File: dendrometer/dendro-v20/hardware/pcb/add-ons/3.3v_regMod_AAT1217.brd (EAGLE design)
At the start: 13.5 x 11.2 mm, 7 parts, among them J1 MF-CON-2.54mm-01x03, J2 CON_01X01LUX, U1 AAT1217-SOT23-6

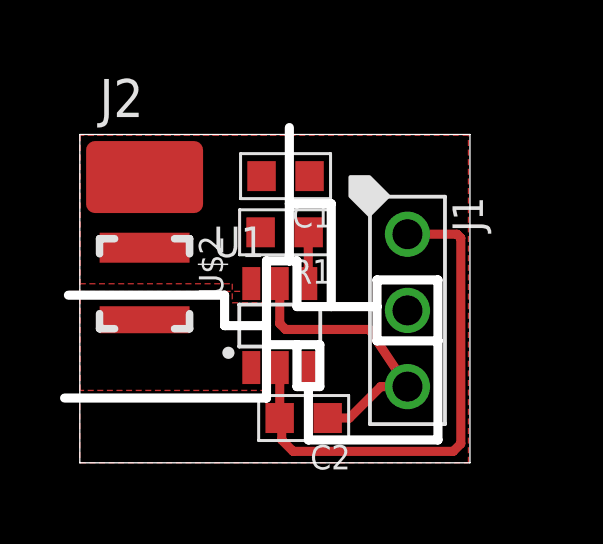
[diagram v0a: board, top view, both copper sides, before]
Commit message: making add-on boards for dendro upgrades)
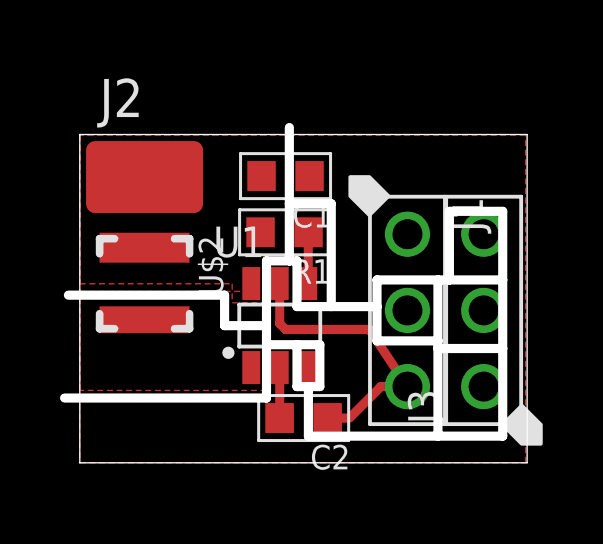
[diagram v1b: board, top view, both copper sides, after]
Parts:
- added J3: MF-CON-2.54mm-01x03, My_Connectors:PTH_2.54MM_01X03
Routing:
- net GND: track 17.4 -> 1.68 mm
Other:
- board size 13.5 x 11.2 mm -> 15.4 x 11.2 mm
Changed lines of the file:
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@@
 <?xml version="1.0" encoding="utf-8"?>
 <!DOCTYPE eagle SYSTEM "eagle.dtd">
-<eagle version="8.0.0">
+<eagle version="8.0.1">
 <drawing>
 <settings>
@@
 <board>
 <plain>
-<wire x1="0" y1="0" x2="13.005" y2="0" width="0" layer="20"/>
-<wire x1="13.005" y1="0" x2="13.005" y2="10.94375" width="0" layer="20"/>
-<wire x1="13.005" y1="10.94375" x2="0" y2="10.94375" width="0" layer="20"/>
+<wire x1="0" y1="0" x2="14.91" y2="0" width="0" layer="20"/>
+<wire x1="14.91" y1="0" x2="14.91" y2="10.94375" width="0" layer="20"/>
+<wire x1="14.91" y1="10.94375" x2="0" y2="10.94375" width="0" layer="20"/>
 <wire x1="0" y1="10.94375" x2="0" y2="0" width="0" layer="20"/>
 <wire x1="-0.381" y1="5.588" x2="4.826" y2="5.588" width="0.3048" layer="46"/>
@@
 <wire x1="9.906" y1="5.207" x2="9.906" y2="4.064" width="0.3048" layer="46"/>
 <wire x1="9.906" y1="4.064" x2="11.938" y2="4.064" width="0.3048" layer="46"/>
-<wire x1="11.938" y1="4.064" x2="11.938" y2="0.762" width="0.3048" layer="46"/>
-<wire x1="11.938" y1="0.762" x2="7.62" y2="0.762" width="0.3048" layer="46"/>
-<wire x1="7.62" y1="0.762" x2="7.62" y2="2.54" width="0.3048" layer="46"/>
+<wire x1="11.938" y1="4.064" x2="11.938" y2="3.81" width="0.3048" layer="46"/>
+<wire x1="11.938" y1="3.81" x2="11.938" y2="0.889" width="0.3048" layer="46"/>
+<wire x1="11.938" y1="0.889" x2="7.62" y2="0.889" width="0.3048" layer="46"/>
+<wire x1="7.62" y1="0.889" x2="7.62" y2="2.54" width="0.3048" layer="46"/>
 <wire x1="9.906" y1="5.207" x2="9.906" y2="6.096" width="0.3048" layer="46"/>
 <wire x1="9.906" y1="6.096" x2="11.938" y2="6.096" width="0.3048" layer="46"/>
 <wire x1="11.938" y1="6.096" x2="11.938" y2="4.064" width="0.3048" layer="46"/>
+<wire x1="14.097" y1="6.096" x2="14.097" y2="3.81" width="0.3048" layer="46"/>
+<wire x1="14.097" y1="3.81" x2="14.097" y2="0.889" width="0.3048" layer="46"/>
+<wire x1="11.938" y1="6.096" x2="12.319" y2="6.096" width="0.3048" layer="46"/>
+<wire x1="12.319" y1="6.096" x2="14.097" y2="6.096" width="0.3048" layer="46"/>
+<wire x1="14.097" y1="0.889" x2="11.938" y2="0.889" width="0.3048" layer="46"/>
+<wire x1="11.938" y1="3.81" x2="14.097" y2="3.81" width="0.3048" layer="46"/>
+<wire x1="12.319" y1="8.382" x2="14.097" y2="8.382" width="0.3048" layer="46"/>
+<wire x1="12.319" y1="8.382" x2="12.319" y2="6.096" width="0.3048" layer="46"/>
+<wire x1="14.097" y1="8.382" x2="14.097" y2="6.096" width="0.3048" layer="46"/>
 </plain>
 <attributes>
@@
 </element>
 <element name="J2" library="My_Connectors" package="1X01_LUXEON-PAD" value="CON_01X01LUX" x="2.159" y="9.525"/>
+<element name="J3" library="My_Connectors" package="PTH_2.54MM_01X03" value="MF-CON-2.54mm-01x03" x="13.462" y="5.08" rot="R90">
+<attribute name="URL" value="https://factory.macrofab.com/part/MF-CON-2.54mm-01x03" x="13.462" y="5.08" size="1.778" layer="27" font="vector" ratio="15" rot="R90" display="off"/>
+<attribute name="MPN" value="MF-CON-2.54mm-01x03" x="13.462" y="5.08" size="1.778" layer="27" font="vector" ratio="15" rot="R90" display="off"/>
+<attribute name="PARTNO" value="" x="13.462" y="5.08" size="1.778" layer="27" font="vector" ratio="15" rot="R90" display="off"/>
+<attribute name="LABEL01" value="" x="13.462" y="5.08" size="1.778" layer="27" font="vector" ratio="15" rot="R90" display="off"/>
+<attribute name="LABEL02" value="" x="13.462" y="5.08" size="1.778" layer="27" font="vector" ratio="15" rot="R90" display="off"/>
+<attribute name="LABEL03" value="" x="13.462" y="5.08" size="1.778" layer="27" font="vector" ratio="15" rot="R90" display="off"/>
+<attribute name="POPULATE" value="1" x="13.462" y="5.08" size="1.778" layer="27" font="vector" ratio="15" rot="R90" display="off"/>
+<attribute name="HOUSEPART" value="YES" x="13.462" y="5.08" size="1.778" layer="27" font="vector" ratio="15" rot="R90" display="off"/>
+</element>
 </elements>
 <signals>
@@
 <polygon width="0.3048" layer="1" isolate="0.3048" thermals="no" rank="6">
 <vertex x="0" y="0"/>
-<vertex x="12.954" y="0"/>
-<vertex x="12.954" y="10.922"/>
+<vertex x="14.859" y="0"/>
+<vertex x="14.859" y="10.922"/>
 <vertex x="0" y="10.922"/>
 </polygon>
 <wire x1="6.665" y1="3.175" x2="6.665" y2="1.496" width="0.3048" layer="1"/>
 <wire x1="6.66125" y1="1.49225" x2="6.665" y2="1.496" width="0.3048" layer="1"/>
-<wire x1="10.922" y1="7.62" x2="12.573" y2="7.62" width="0.3048" layer="1"/>
-<wire x1="12.573" y1="7.62" x2="12.7" y2="7.493" width="0.3048" layer="1"/>
-<wire x1="12.7" y1="7.493" x2="12.7" y2="0.635" width="0.3048" layer="1"/>
-<wire x1="12.7" y1="0.635" x2="12.446" y2="0.381" width="0.3048" layer="1"/>
-<wire x1="12.446" y1="0.381" x2="7.112" y2="0.381" width="0.3048" layer="1"/>
-<wire x1="7.112" y1="0.381" x2="6.731" y2="0.762" width="0.3048" layer="1"/>
-<wire x1="6.731" y1="0.762" x2="6.731" y2="1.4225" width="0.3048" layer="1"/>
-<wire x1="6.731" y1="1.4225" x2="6.66125" y2="1.49225" width="0.3048" layer="1"/>
+<wire x1="6.665" y1="3.175" x2="10.922" y2="7.62" width="0" layer="19" extent="1-1"/>
 </signal>
 <signal name="3V3">
